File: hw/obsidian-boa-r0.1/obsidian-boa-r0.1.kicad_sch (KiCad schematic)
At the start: 87 parts, among them J1 USB_C, J2 PROG, P0 0, P1 1, P10 10, P11 11, P12 12, P13 13, P14 14, P15 15, P16 16, P17 17, P18 18, P19 19, P2 2, P20 20, P21 21, P22 22, P23 23, P24 GND, P25 GND, P26 GND, P27 3V3, P28 3V3, P29 VIN, P3 3, P30 CDONE, P31 CRESET, P32 UP, P33 UP, P34 UP, P35 UP, P4 4, P5 5, P6 6, P7 7, P8 8, P9 9, SW1 TACT, U1 USBLC6-2, U2 W25Q32JVSS, U3 ESP32-S2, U4 W25Q32JVSS, U5 TPS62290, Y1 40MHz

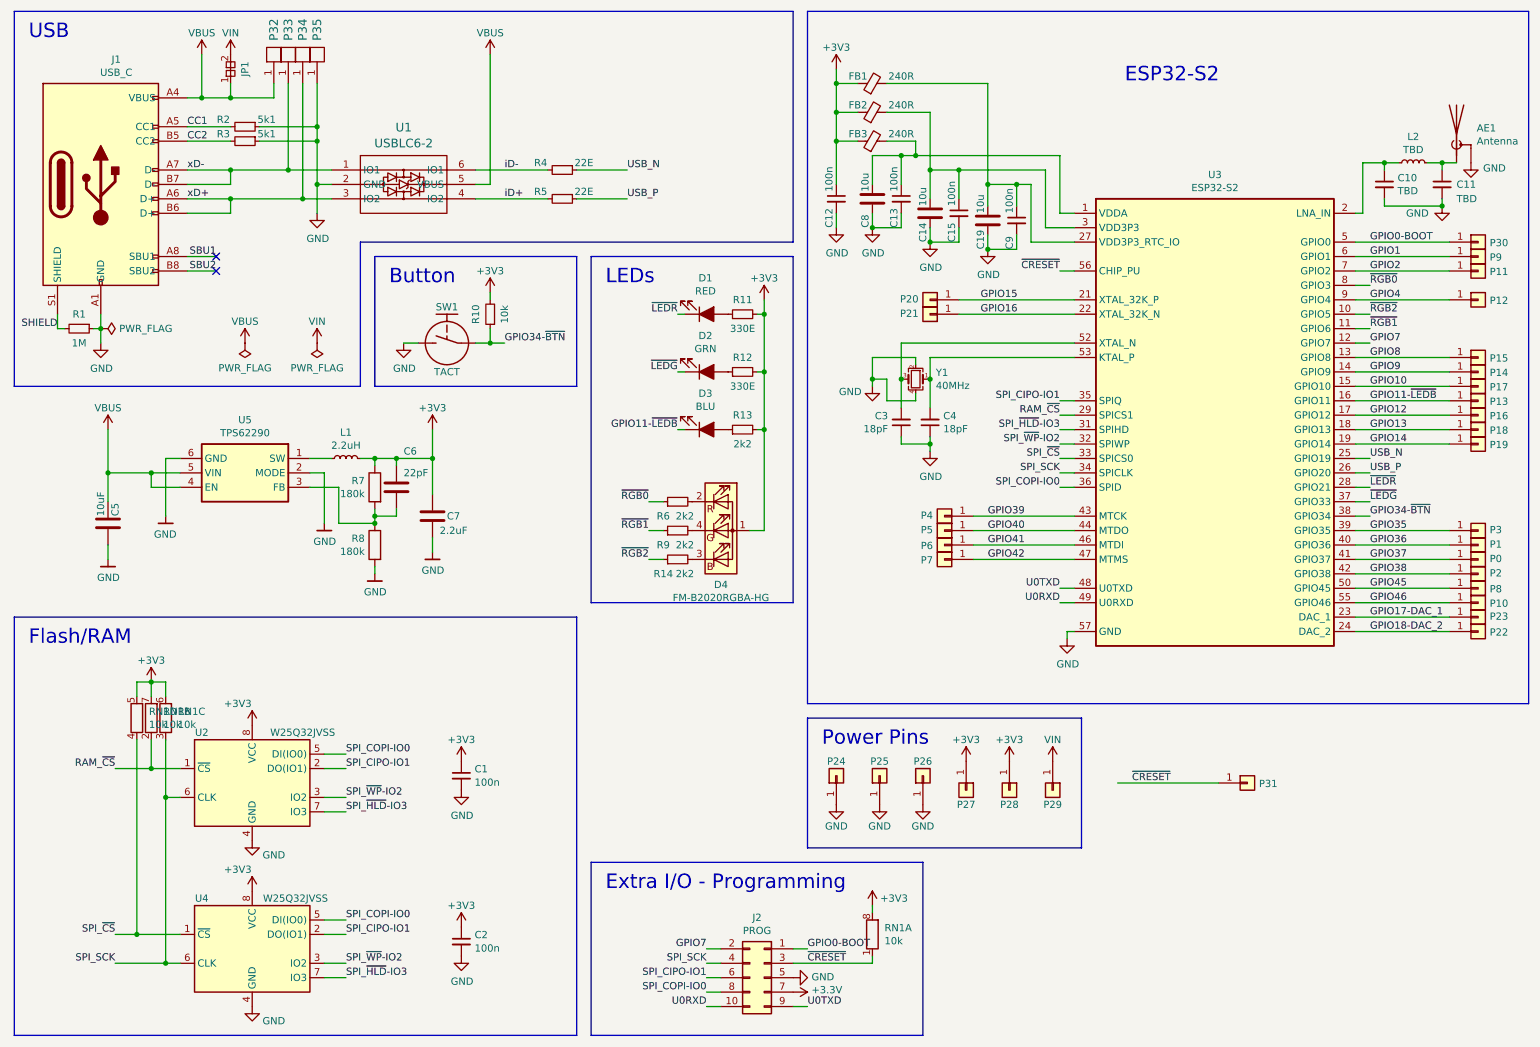
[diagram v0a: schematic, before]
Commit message: hw.r0d1: update to route VDD_SPI seperately.
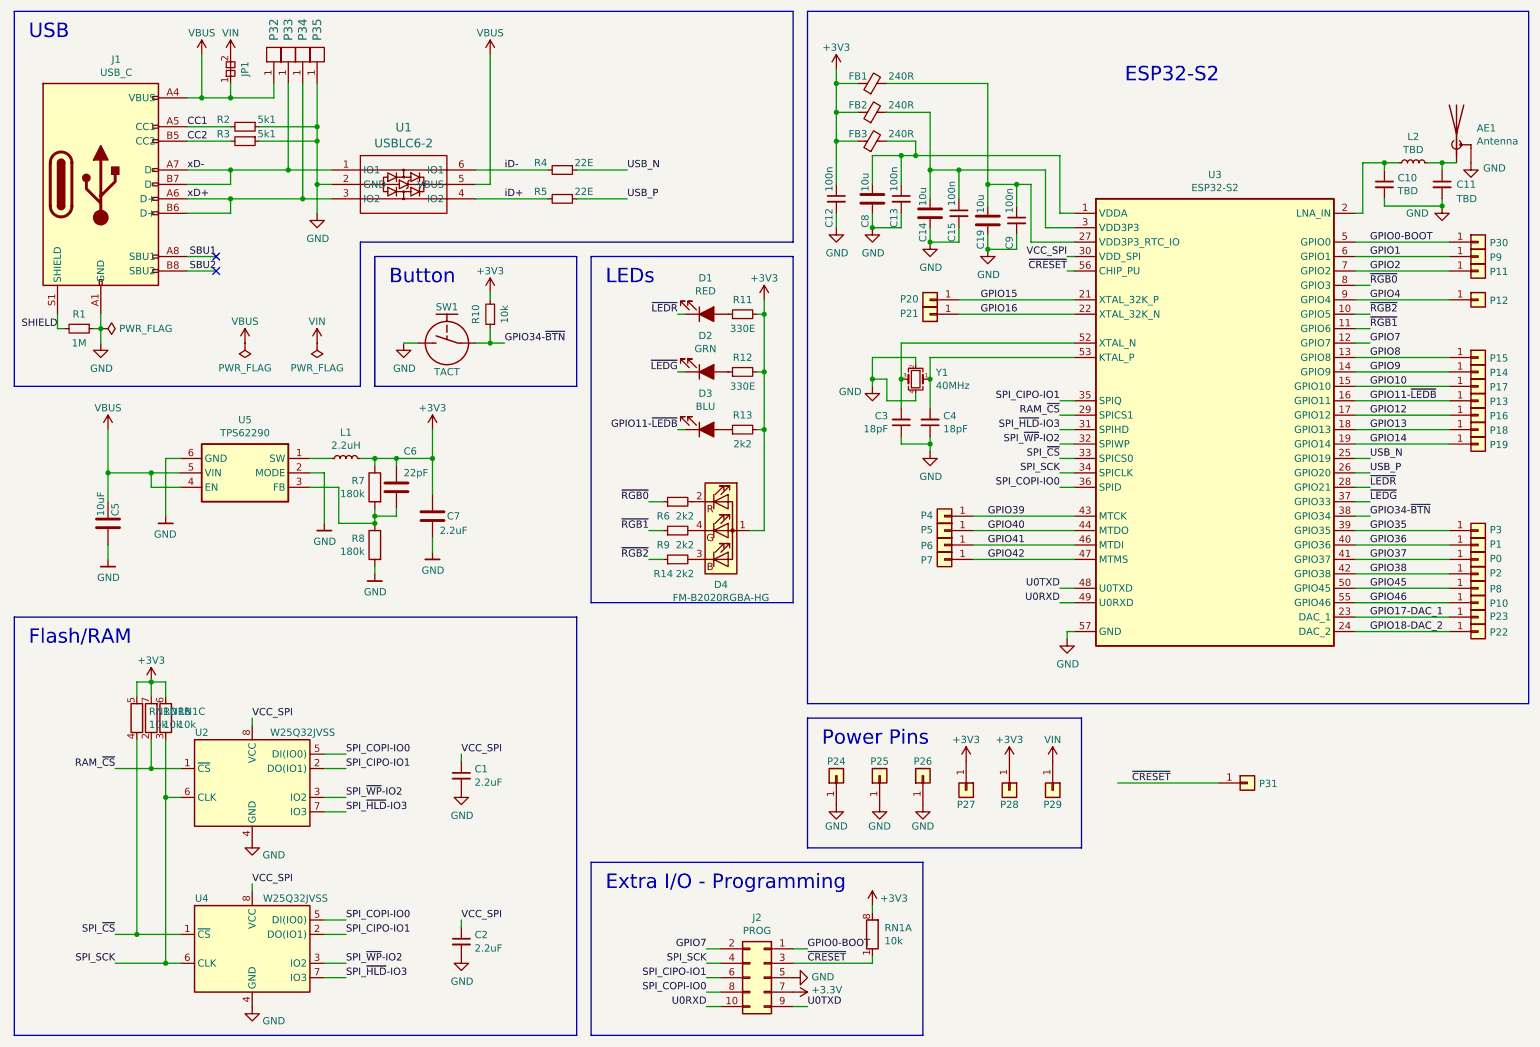
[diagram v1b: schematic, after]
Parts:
- C1, C2: value 100n -> 2.2uF
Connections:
- net +3V3: no longer C1.1, C2.1, U2.8 (VCC), U4.8 (VCC)
- net at C19.1, C9.1, FB1.2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: no longer U3.30 (VDD_SPI)
- new net VCC_SPI: C1.1, C2.1, U2.8 (VCC), U3.30 (VDD_SPI), U4.8 (VCC)
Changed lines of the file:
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@@
     (stroke (width 0) (type solid) (color 0 0 0 0))
   )
+  (wire (pts (xy 57.15 139.7) (xy 57.15 140.97))
+    (stroke (width 0) (type solid) (color 0 0 0 0))
+  )
+  (wire (pts (xy 57.15 168.91) (xy 57.15 170.18))
+    (stroke (width 0) (type solid) (color 0 0 0 0))
+  )
   (wire (pts (xy 58.42 35.56) (xy 68.58 35.56))
     (stroke (width 0) (type solid) (color 0 0 0 0))
@@
     (stroke (width 0) (type solid) (color 0 0 0 0))
   )
+  (wire (pts (xy 93.98 146.05) (xy 93.98 147.32))
+    (stroke (width 0) (type solid) (color 0 0 0 0))
+  )
+  (wire (pts (xy 93.98 175.26) (xy 93.98 176.53))
+    (stroke (width 0) (type solid) (color 0 0 0 0))
+  )
   (wire (pts (xy 96.52 43.18) (xy 109.22 43.18))
     (stroke (width 0) (type solid) (color 0 0 0 0))
@@
     (stroke (width 0) (type solid) (color 0 0 0 0))
   )
-  (wire (pts (xy 199.39 60.96) (xy 201.93 60.96))
+  (wire (pts (xy 200.66 58.42) (xy 201.93 58.42))
+    (stroke (width 0) (type solid) (color 0 0 0 0))
+  )
+  (wire (pts (xy 200.66 60.96) (xy 201.93 60.96))
     (stroke (width 0) (type solid) (color 0 0 0 0))
   )
@@
     (effects (font (size 1.27 1.27)) (justify right bottom))
   )
+  (label "VCC_SPI" (at 57.15 139.7 0)
+    (effects (font (size 1.27 1.27)) (justify left bottom))
+  )
+  (label "VCC_SPI" (at 57.15 168.91 0)
+    (effects (font (size 1.27 1.27)) (justify left bottom))
+  )
   (label "SPI_COPI-IO0" (at 73.66 146.05 0)
     (effects (font (size 1.27 1.27)) (justify left bottom))
@@
     (effects (font (size 1.27 1.27)) (justify left bottom))
   )
+  (label "VCC_SPI" (at 93.98 146.05 0)
+    (effects (font (size 1.27 1.27)) (justify left bottom))
+  )
+  (label "VCC_SPI" (at 93.98 175.26 0)
+    (effects (font (size 1.27 1.27)) (justify left bottom))
+  )
   (label "iD-" (at 101.6 43.18 0)
     (effects (font (size 1.27 1.27)) (justify left bottom))
@@
     (effects (font (size 1.27 1.27)) (justify left bottom))
   )
-  (label "~CRESET" (at 199.39 60.96 180)
-    (effects (font (size 1.27 1.27)) (justify right bottom))
-  )
   (label "SPI_CIPO-IO1" (at 199.39 83.82 180)
     (effects (font (size 1.27 1.27)) (justify right bottom))
@@
     (effects (font (size 1.27 1.27)) (justify right bottom))
   )
+  (label "VCC_SPI" (at 200.66 58.42 180)
+    (effects (font (size 1.27 1.27)) (justify right bottom))
+  )
+  (label "~CRESET" (at 200.66 60.96 180)
+    (effects (font (size 1.27 1.27)) (justify right bottom))
+  )
   (label "~CRESET" (at 212.09 151.13 0)
     (effects (font (size 1.27 1.27)) (justify left bottom))
@@
     )
   )
-  (symbol (lib_id "power:+3V3") (at 57.15 140.97 0) (unit 1)
-    (in_bom yes) (on_board yes)
-    (property "Reference" "#PWR0116" (id 0) (at 57.15 144.78 0)
-      (effects (font (size 1.27 1.27)) hide)
-    )
-    (property "Value" "+3V3" (id 1) (at 54.61 137.16 0))
-    (property "Footprint" "" (id 2) (at 57.15 140.97 0)
-      (effects (font (size 1.27 1.27)) hide)
-    )
-    (property "Datasheet" "" (id 3) (at 57.15 140.97 0)
-      (effects (font (size 1.27 1.27)) hide)
-    )
-  )
-  (symbol (lib_id "power:+3V3") (at 57.15 170.18 0) (unit 1)
-    (in_bom yes) (on_board yes)
-    (property "Reference" "#PWR0129" (id 0) (at 57.15 173.99 0)
-      (effects (font (size 1.27 1.27)) hide)
-    )
-    (property "Value" "+3V3" (id 1) (at 54.61 166.37 0))
-    (property "Footprint" "" (id 2) (at 57.15 170.18 0)
-      (effects (font (size 1.27 1.27)) hide)
-    )
-    (property "Datasheet" "" (id 3) (at 57.15 170.18 0)
-      (effects (font (size 1.27 1.27)) hide)
-    )
-  )
   (symbol (lib_id "icebreaker-bitsy-rescue:VIN-pkl_power") (at 68.58 73.66 0) (unit 1)
     (in_bom yes) (on_board yes)
@@
     )
   )
-  (symbol (lib_id "power:+3V3") (at 93.98 147.32 0) (unit 1)
-    (in_bom yes) (on_board yes)
-    (property "Reference" "#PWR0130" (id 0) (at 93.98 151.13 0)
-      (effects (font (size 1.27 1.27)) hide)
-    )
-    (property "Value" "+3V3" (id 1) (at 93.98 143.51 0))
-    (property "Footprint" "" (id 2) (at 93.98 147.32 0)
-      (effects (font (size 1.27 1.27)) hide)
-    )
-    (property "Datasheet" "" (id 3) (at 93.98 147.32 0)
-      (effects (font (size 1.27 1.27)) hide)
-    )
-  )
-  (symbol (lib_id "power:+3V3") (at 93.98 176.53 0) (unit 1)
-    (in_bom yes) (on_board yes)
-    (property "Reference" "#PWR0114" (id 0) (at 93.98 180.34 0)
-      (effects (font (size 1.27 1.27)) hide)
-    )
-    (property "Value" "+3V3" (id 1) (at 93.98 172.72 0))
-    (property "Footprint" "" (id 2) (at 93.98 176.53 0)
-      (effects (font (size 1.27 1.27)) hide)
-    )
-    (property "Datasheet" "" (id 3) (at 93.98 176.53 0)
-      (effects (font (size 1.27 1.27)) hide)
-    )
-  )
   (symbol (lib_id "power:VBUS") (at 99.06 22.86 0) (unit 1)
     (in_bom yes) (on_board yes)
@@
       (effects (font (size 1.27 1.27)) (justify left))
     )
-    (property "Value" "100n" (id 1) (at 96.3168 151.0284 0)
+    (property "Value" "2.2uF" (id 1) (at 96.3168 151.0284 0)
       (effects (font (size 1.27 1.27)) (justify left))
     )
@@
       (effects (font (size 1.27 1.27)) (justify left))
     )
-    (property "Value" "100n" (id 1) (at 96.3168 180.2384 0)
+    (property "Value" "2.2uF" (id 1) (at 96.3168 180.2384 0)
       (effects (font (size 1.27 1.27)) (justify left))
     )
@@
       (reference "#PWR0113") (unit 1)
     )
-    (path "/28ad995f-f72b-470a-b8dc-388df300654d"
-      (reference "#PWR0114") (unit 1)
-    )
     (path "/821c1052-0fb1-4037-9de7-c2e9c45a8eb0"
       (reference "#PWR0115") (unit 1)
     )
-    (path "/30484aa8-22ce-4902-b099-9ad3ddb6dd07"
-      (reference "#PWR0116") (unit 1)
-    )
     (path "/00000000-0000-0000-0000-00005f458f8a"
       (reference "#PWR0117") (unit 1)
@@
       (reference "#PWR0128") (unit 1)
     )
-    (path "/2cfb2602-5c76-4bff-92b2-1415243e18aa"
-      (reference "#PWR0129") (unit 1)
-    )
-    (path "/45190b80-de86-4d13-8640-3130129411b8"
-      (reference "#PWR0130") (unit 1)
-    )
     (path "/16bfcbeb-b535-4c02-87af-5390e4aa2c69"

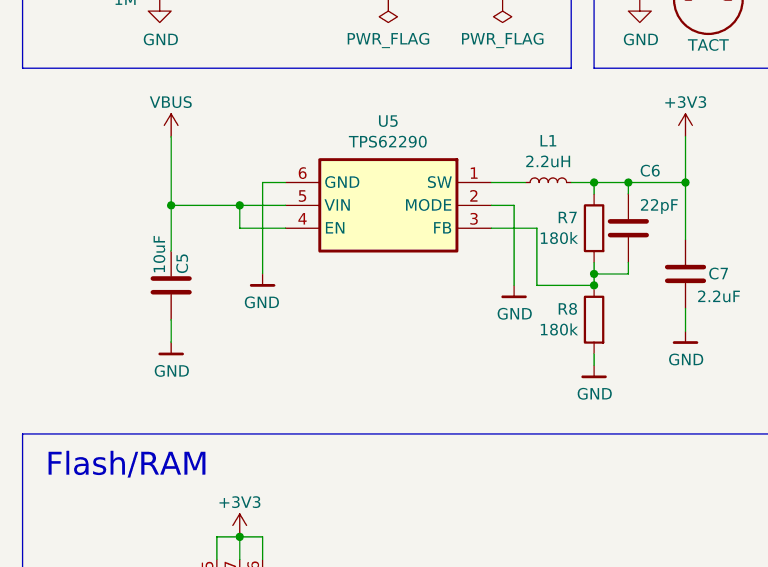
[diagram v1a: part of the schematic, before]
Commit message: hw.r0d1: Update BOM fields
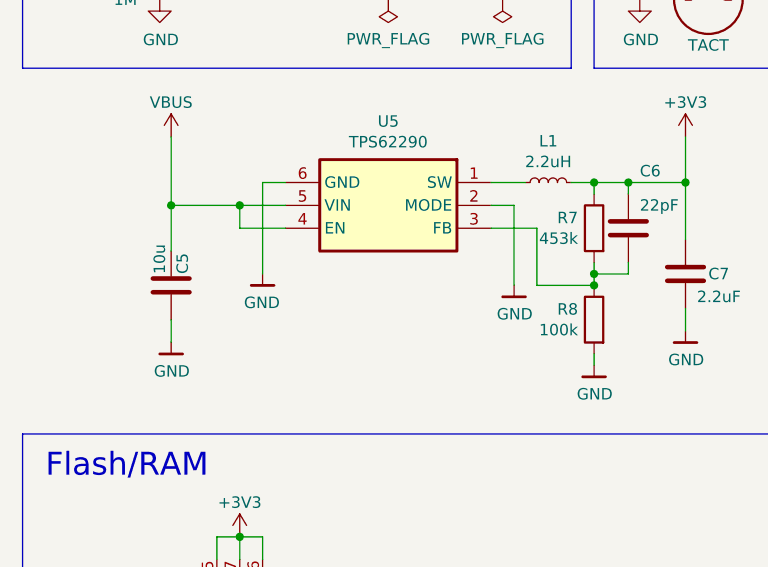
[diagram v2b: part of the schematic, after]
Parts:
- AE1: Mfg (none) -> Molex; PN (none) -> 0479480001
- C1, C2: Key cap-cer-0402-100n -> (none); Mfg (none) -> Yageo; PN (none) -> CC0402MRX5R5BB225; Source ANY -> (none)
- C10, C11: Key cap-cer-0402-100n -> (none)
- C12, C13, C15, C9: Key cap-cer-0402-100n -> (none); Mfg (none) -> Yageo; PN (none) -> CC0402ZRY5V7BB104; Source ANY -> (none)
- C14, C19, C8: Key cap-cer-0603-10u -> (none); Mfg (none) -> Yageo; PN (none) -> CC0603KRX5R5BB106; Source ANY -> (none)
- C3, C4: Key cap-cer-0402-100n -> (none); Mfg (none) -> Yageo; PN (none) -> CC0402GRNPO9BN180; Source ANY -> (none)
- C5: value 10uF -> 10u; Mfg Samsung Electro-Mechanics -> Yageo; PN CL05B104KP5NNNC -> CC0603KRX5R5BB106
- C6: Mfg Samsung Electro-Mechanics -> Yageo; PN CL05B104KP5NNNC -> CC0402KRNPO9BN220
- C7: Mfg Samsung Electro-Mechanics -> Yageo; PN CL05B104KP5NNNC -> CC0402MRX5R5BB225
- D1: Key led-0603-red -> (none); Mfg (none) -> Lite-On Inc.; PN (none) -> LTST-C191KRKT; Source ANY -> (none)
- D2: Key led-0603-grn -> (none); Mfg (none) -> Lite-On Inc.; PN (none) -> LTST-C191KGKT; Source ANY -> (none)
- D3: Key led-0603-blu -> (none); Mfg (none) -> Lite-On Inc.; PN (none) -> LTST-C191TBKT; Source ANY -> (none)
- D4: Key led-1010-rgb -> (none)
- FB1, FB2, FB3: Mfg (none) -> Murata Electronics; PN (none) -> BLM15BC241SN1D
- J1: Mfg (none) -> GCT; PN (none) -> USB4105-GF-A
- R1: Key res-0402-1m -> (none); Mfg (none) -> Yageo; PN (none) -> RC0402FR-071ML; Source ANY -> (none)
- R10: Key res-0402-10k -> (none); Mfg (none) -> Yageo; PN (none) -> RC0402FR-0710KL; Source ANY -> (none)
- R11, R12: Key res-0402-330 -> (none); Mfg (none) -> Yageo; PN (none) -> RC0402FR-07330RL; Source ANY -> (none)
- R13, R14, R6, R9: Key res-0402-2k2 -> (none); Mfg (none) -> Yageo; PN (none) -> RC0402FR-072K2L; Source ANY -> (none)
- R2, R3: Key res-0402-1m -> (none); Mfg (none) -> Yageo; PN (none) -> RC0402FR-075K1L; Source ANY -> (none)
- R4, R5: Key res-0402-22 -> (none); Mfg (none) -> Yageo; PN (none) -> RC0402FR-0722RL; Source ANY -> (none)
- R7: value 180k -> 453k; Mfg (none) -> Yageo; PN (none) -> RC0402FR-07453KL
- R8: value 180k -> 100k; Mfg (none) -> Yageo; PN (none) -> RC0402FR-07100KL
- SW1: Key sw-tact-top-4.2-2.8 -> (none)
- U1: Key tvs-diode-sot666 -> (none); Mfg (none) -> STMicroelectronics; PN (none) -> USBLC6-2P6; Source ANY -> (none)
- U3: Mfg (none) -> Espressif Systems; PN (none) -> ESP32-S2
- U4: Mfg (none) -> Winbond Electronics; PN (none) -> W25Q128JVSIQ TR
- U5: Mfg (none) -> Texas Instruments; PN (none) -> TPS62290DRVR
- Y1: Mfg (none) -> ECS Inc.; PN (none) -> ECS-400-10-36B-CKY-TR
